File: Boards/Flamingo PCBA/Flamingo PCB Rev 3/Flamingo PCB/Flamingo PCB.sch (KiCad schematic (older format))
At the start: 0 parts

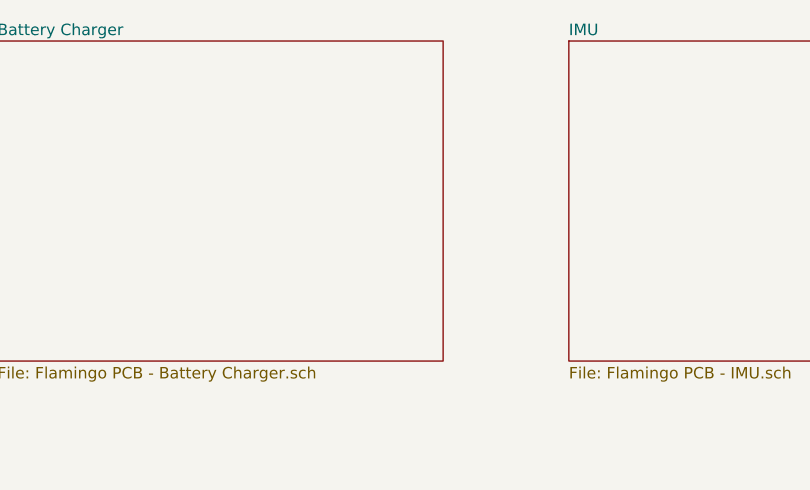
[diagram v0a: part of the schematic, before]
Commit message: PCB: bringing in symbols, re-making battery charger sheet, still has todo
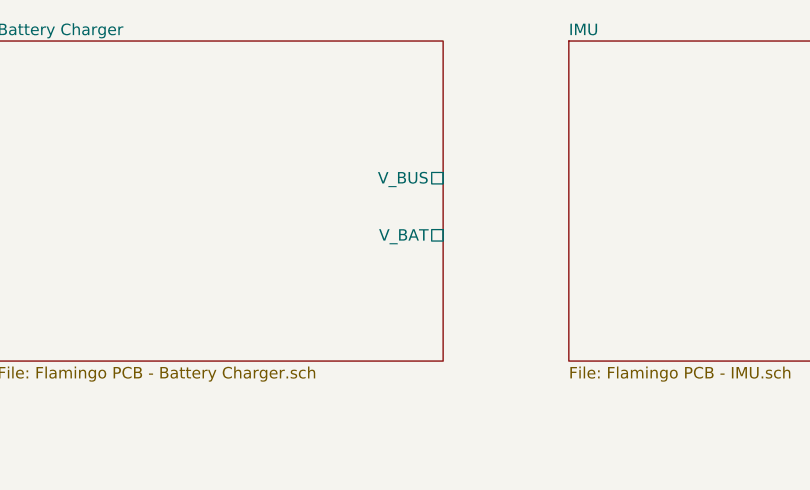
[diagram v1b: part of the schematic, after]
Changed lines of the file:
@@
 $Descr USLetter 11000 8500
 encoding utf-8
-Sheet 1 4
+Sheet 1 5
 Title "Flamingo PCB"
 Date "2020-09-29"
@@
 F0 "Battery Charger" 50
 F1 "Flamingo PCB - Battery Charger.sch" 50
+F2 "V_BAT" U R 5950 2350 50
+F3 "V_BUS" U R 5950 2100 50
 $EndSheet
 $Sheet

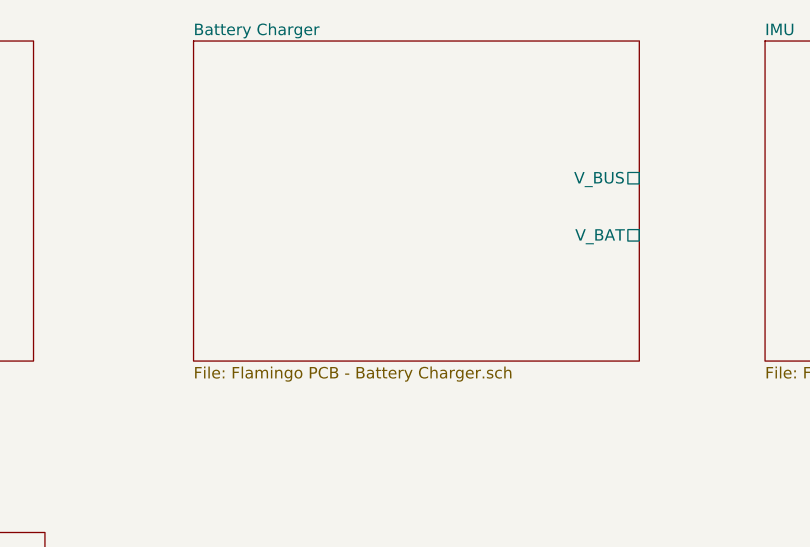
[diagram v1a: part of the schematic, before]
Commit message: Changed ATMEGA328P for a modified DK symbol
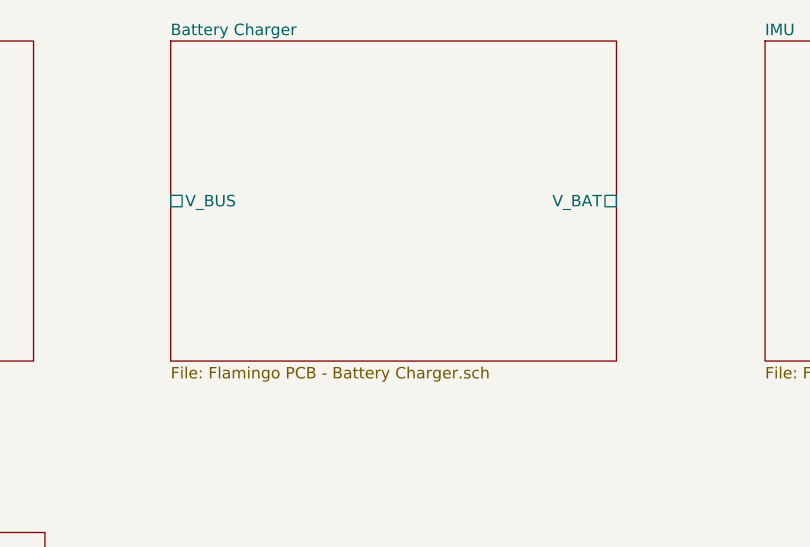
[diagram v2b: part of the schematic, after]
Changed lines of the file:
@@
 $EndSheet
 $Sheet
-S 4000 1500 1950 1400
+S 3900 1500 1950 1400
 U 5F780D75
 F0 "Battery Charger" 50
 F1 "Flamingo PCB - Battery Charger.sch" 50
-F2 "V_BAT" U R 5950 2350 50
-F3 "V_BUS" U R 5950 2100 50
+F2 "V_BAT" U R 5850 2200 50
+F3 "V_BUS" U L 3900 2200 50
 $EndSheet
 $Sheet

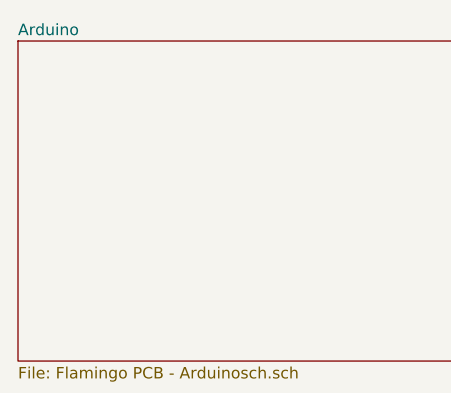
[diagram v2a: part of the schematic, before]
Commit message: Worked on Power board mainly.
Still have to resolve the power sharing.
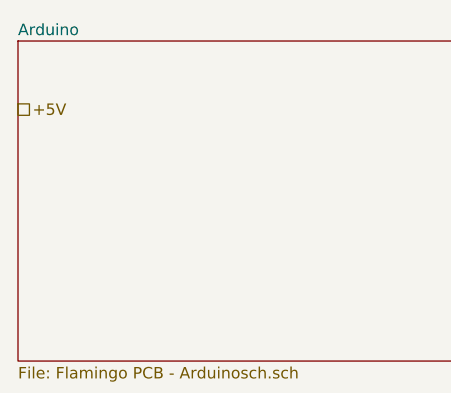
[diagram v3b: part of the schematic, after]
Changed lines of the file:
@@
 F1 "Flamingo PCB - Power.sch" 50
 $EndSheet
+Text HLabel 1300 1800 2    50   UnSpc ~ 0
++5V
 $EndSCHEMATC

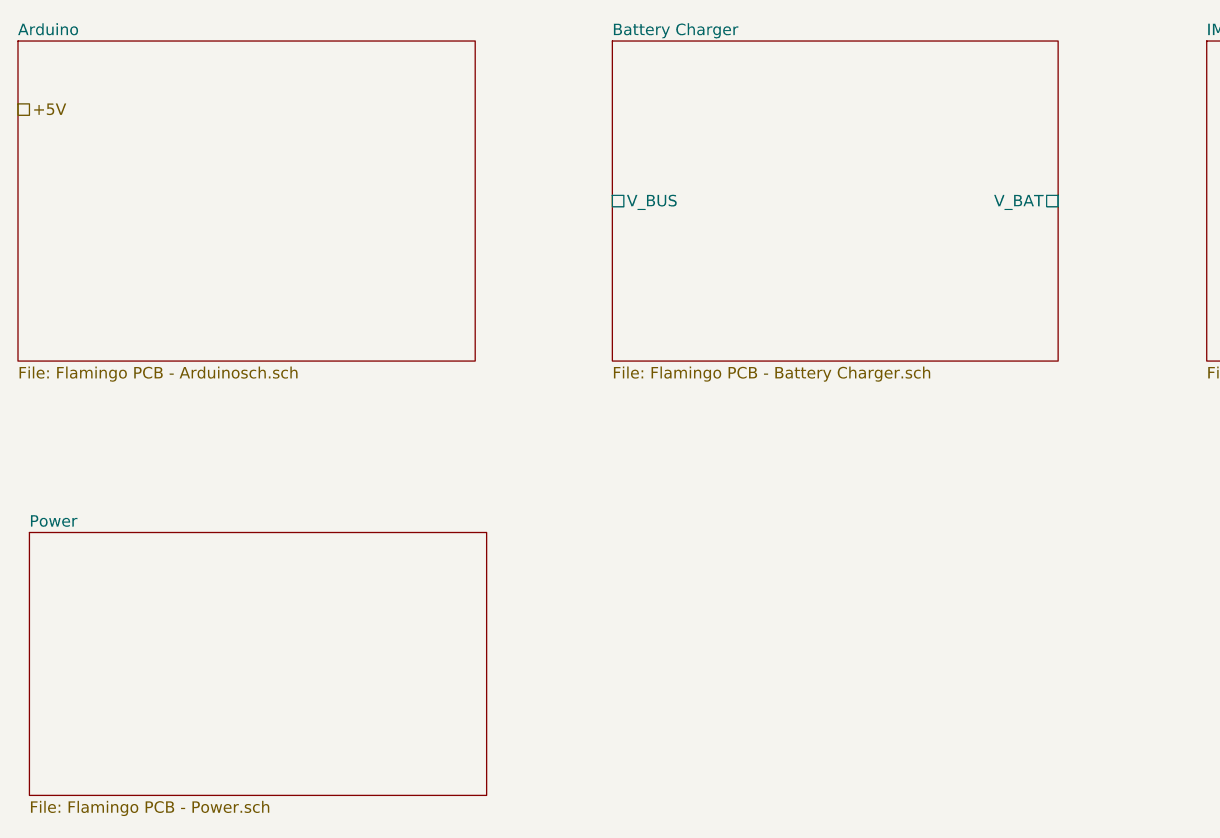
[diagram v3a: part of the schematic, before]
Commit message: Tidied up Power schematic, trying for load switching P-channel MOSFET
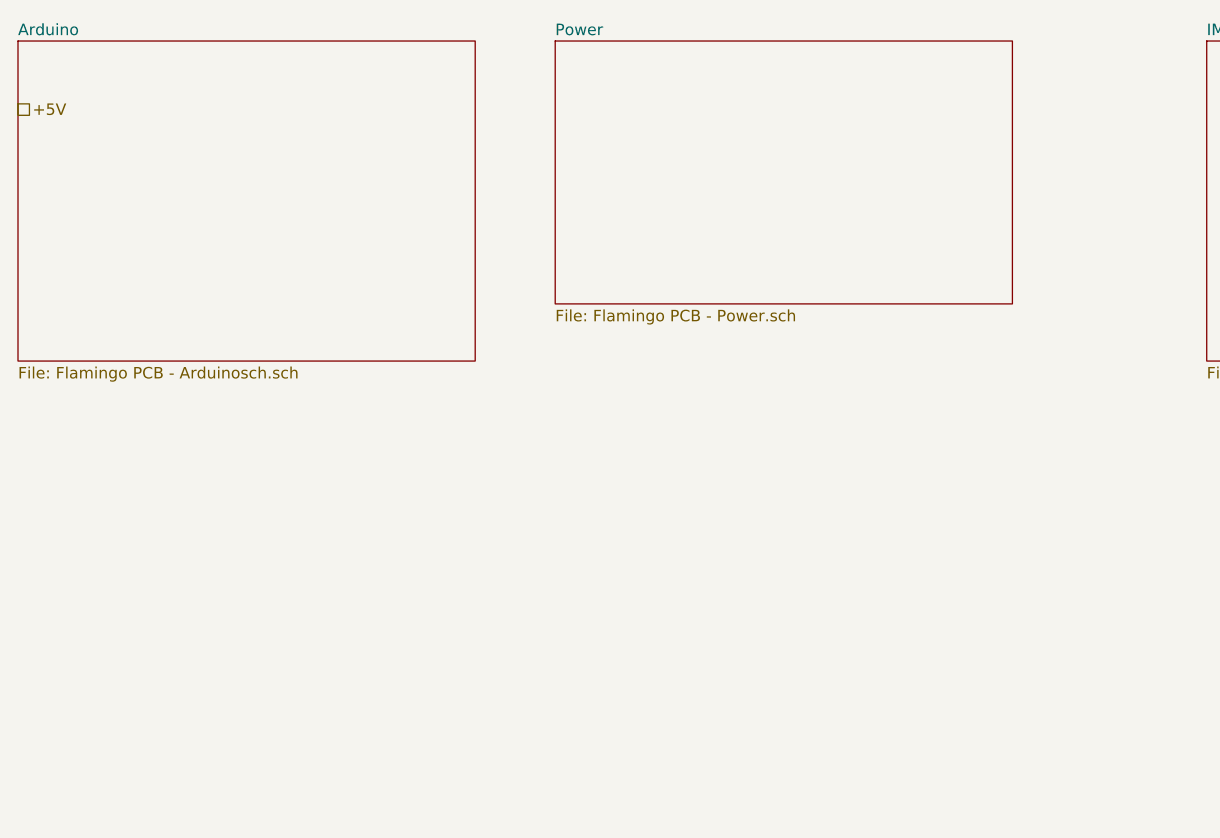
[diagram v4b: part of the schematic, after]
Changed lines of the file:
@@
 $Descr USLetter 11000 8500
 encoding utf-8
-Sheet 1 5
+Sheet 1 4
 Title "Flamingo PCB"
 Date "2020-09-29"
@@
 $EndSheet
 $Sheet
-S 3900 1500 1950 1400
-U 5F780D75
-F0 "Battery Charger" 50
-F1 "Flamingo PCB - Battery Charger.sch" 50
-F2 "V_BAT" U R 5850 2200 50
-F3 "V_BUS" U L 3900 2200 50
-$EndSheet
-$Sheet
 S 6500 1500 2000 1400
 U 5F780E58
@@
 $EndSheet
 $Sheet
-S 1350 3650 2000 1150
+S 3650 1500 2000 1150
 U 5F780F7E
 F0 "Power" 50

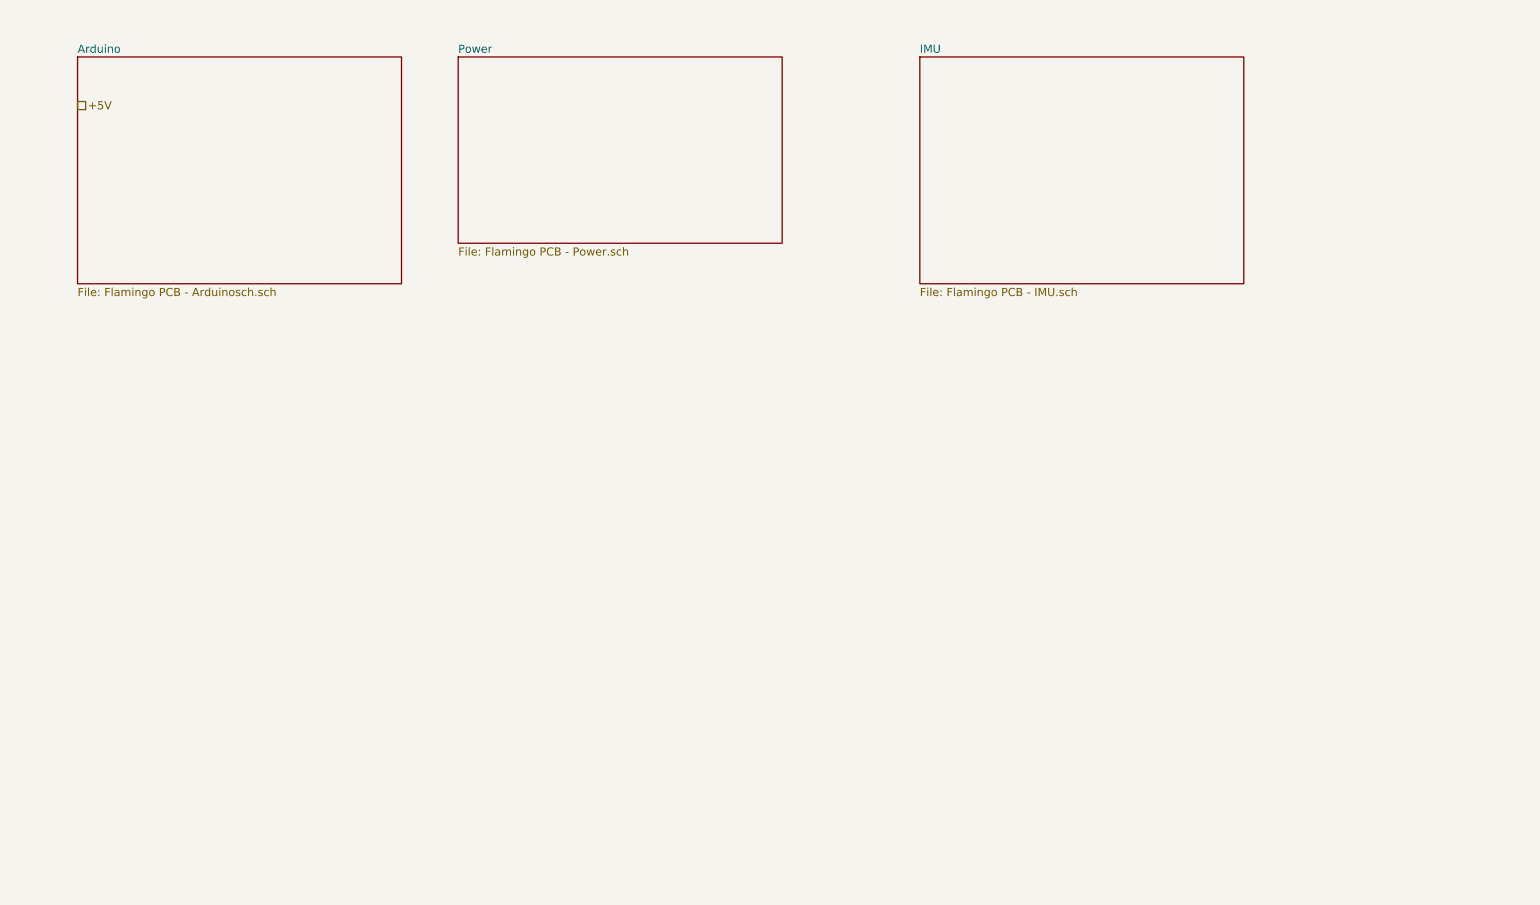
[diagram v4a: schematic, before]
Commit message: More work on Arduino schematic, created button board schematic
Button board schematic should probably be a separate project
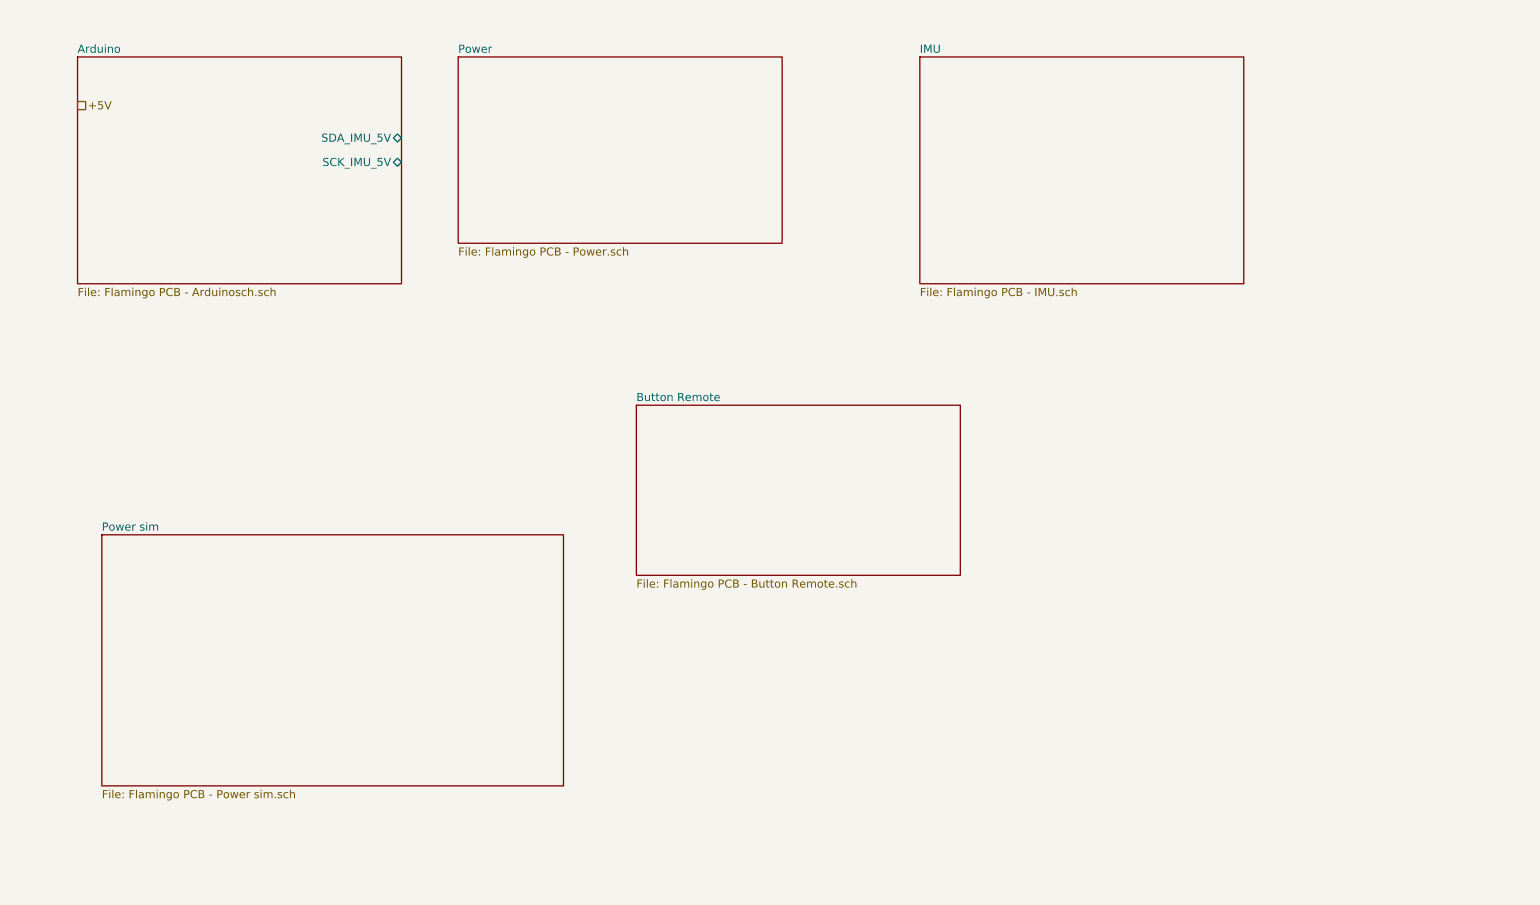
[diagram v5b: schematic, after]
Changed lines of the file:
@@
 $Descr USLetter 11000 8500
 encoding utf-8
-Sheet 1 4
+Sheet 1 6
 Title "Flamingo PCB"
 Date "2020-09-29"
@@
 F0 "Arduino" 50
 F1 "Flamingo PCB - Arduinosch.sch" 50
+F2 "SDA_IMU_5V" B R 3300 2000 50
+F3 "SCK_IMU_5V" B R 3300 2150 50
 $EndSheet
 $Sheet
@@
 Text HLabel 1300 1800 2    50   UnSpc ~ 0
 +5V
+$Sheet
+S 1450 4450 2850 1550
+U 5F85F8A8
+F0 "Power sim" 50
+F1 "Flamingo PCB - Power sim.sch" 50
+$EndSheet
+$Sheet
+S 4750 3650 2000 1050
+U 5FA54816
+F0 "Button Remote" 50
+F1 "Flamingo PCB - Button Remote.sch" 50
+$EndSheet
 $EndSCHEMATC

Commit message: Tidy up
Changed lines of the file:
@@
 $Descr USLetter 11000 8500
 encoding utf-8
-Sheet 1 6
+Sheet 1 5
 Title "Flamingo PCB"
 Date "2020-09-29"
@@
 +5V
 $Sheet
-S 1450 4450 2850 1550
-U 5F85F8A8
-F0 "Power sim" 50
-F1 "Flamingo PCB - Power sim.sch" 50
-$EndSheet
-$Sheet
-S 4750 3650 2000 1050
+S 7050 4850 2000 1050
 U 5FA54816
 F0 "Button Remote" 50
